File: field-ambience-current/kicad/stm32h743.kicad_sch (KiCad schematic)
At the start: 33 parts, among them J10 3.5mm TRS MIDI-Out (Type A, P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, J4 SWD 1.27mm (SWCLK/GND/SWDIO), U1 STM32H743VIT6 (480MHz M7, LQF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, Y1 8MHz ABLS-8.000MHZ-B4-T (CL=1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

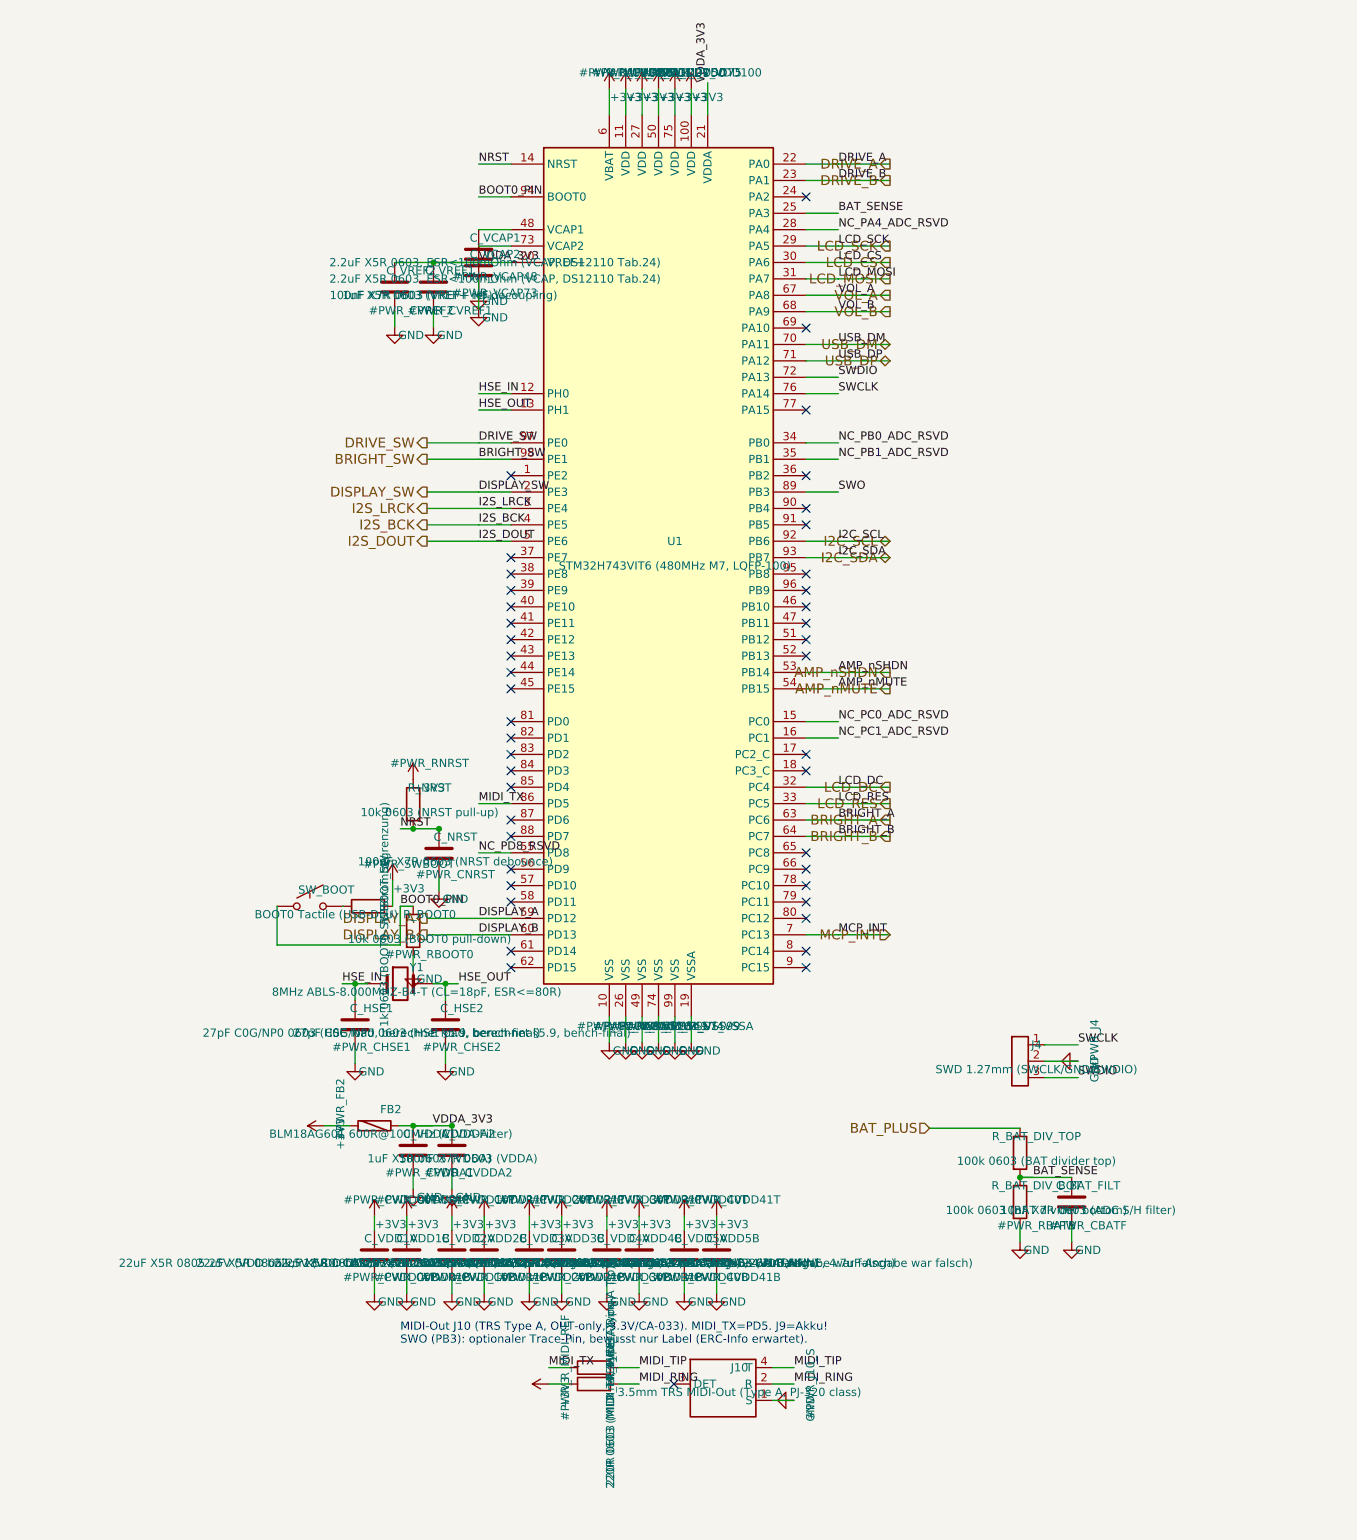
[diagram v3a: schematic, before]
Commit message: feat(hw): QSPI-PSRAM 8MB (APS6404L) into the schematic on QUADSPI BK2 (r19.10)
* feat(hw): QSPI-PSRAM (8MB) into the schematic — U9 APS6404L on QUADSPI BK2 (r19.10)

Implements ADR-0022. The internal RAM is the wall for "maximum sound"
(D1/D2 at 96%); this adds an external 8 MB QSPI PSRAM, memory-mapped over
QUADSPI Bank 2, so the CPU reads it like internal RAM (behind the D-cache).
Enables sample playback, convolution reverb with real IRs, big granular,
and a true multi-table Blendwave — megabytes instead of kilobytes.

Generator (generate_kicad_project.py, stm32h743 sheet):
- New lib_symbol Memory_RAM:APS6404L (SOP-8). Pinout VERIFIED against the AP
  Memory datasheet Rev 2.1 (2019), top view: 1=/CE 2=SO/SIO1 3=SIO2 4=VSS
  5=SI/SIO0 6=SCLK 7=SIO3 8=VDD.
- U9 APS6404L-3SQR-SN, FP Package_SO:SOIC-8_3.9x4.9mm_P1.27mm (dimensionally
  matches SOP-8L(150) = 3.9mm body / 1.27mm pitch; standard SOIC pad
  numbering), LCSC C5333729. FP_NOTE recommends pulling the exact LCSC land
  pattern via easyeda2kicad as a belt-and-suspenders final check.
- 6 QSPI nets on the MCU pins PB2(36)/PC11(79)/PE7-10(37-40):
  QSPI_CLK/QSPI_NCS/QSPI_IO0-3, wired both sides by local label.
- Decoupling C_QSPI 100nF (C14663) + C_QSPI2 10uF (C15850) to +3V3/GND;
  U9 VDD->+3V3, VSS->GND.

Docs/BOM:
- PINMAP: PB2/PC11/PE7-10 marked as QSPI (no longer free) + connectivity
  table; fixed ADR "Pin 80" -> PC11 is LQFP100 pin 79 (pin 80 = PC12).
- jlc_bom.csv regenerated (U9 + 2 caps flow from the schematic).
- bom_overview.html: new "Memory" group; U9 badge honestly "JLC ? verify"
  (JLC-Economic assemblable per ADR — verify live before order).
- ADR-0022 -> IMPLEMENTED with datasheet-verified pinout + Verifikation.

Verification: kicad-cli 7.0.11 in this environment cannot load the
generated schematic (Failed to load schematic file — reproduced on the
UNCHANGED baseline via git stash, so it is a pre-existing parser
incompatibility, not this change) and has no `sch erc` subcommand. Verified
at text 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
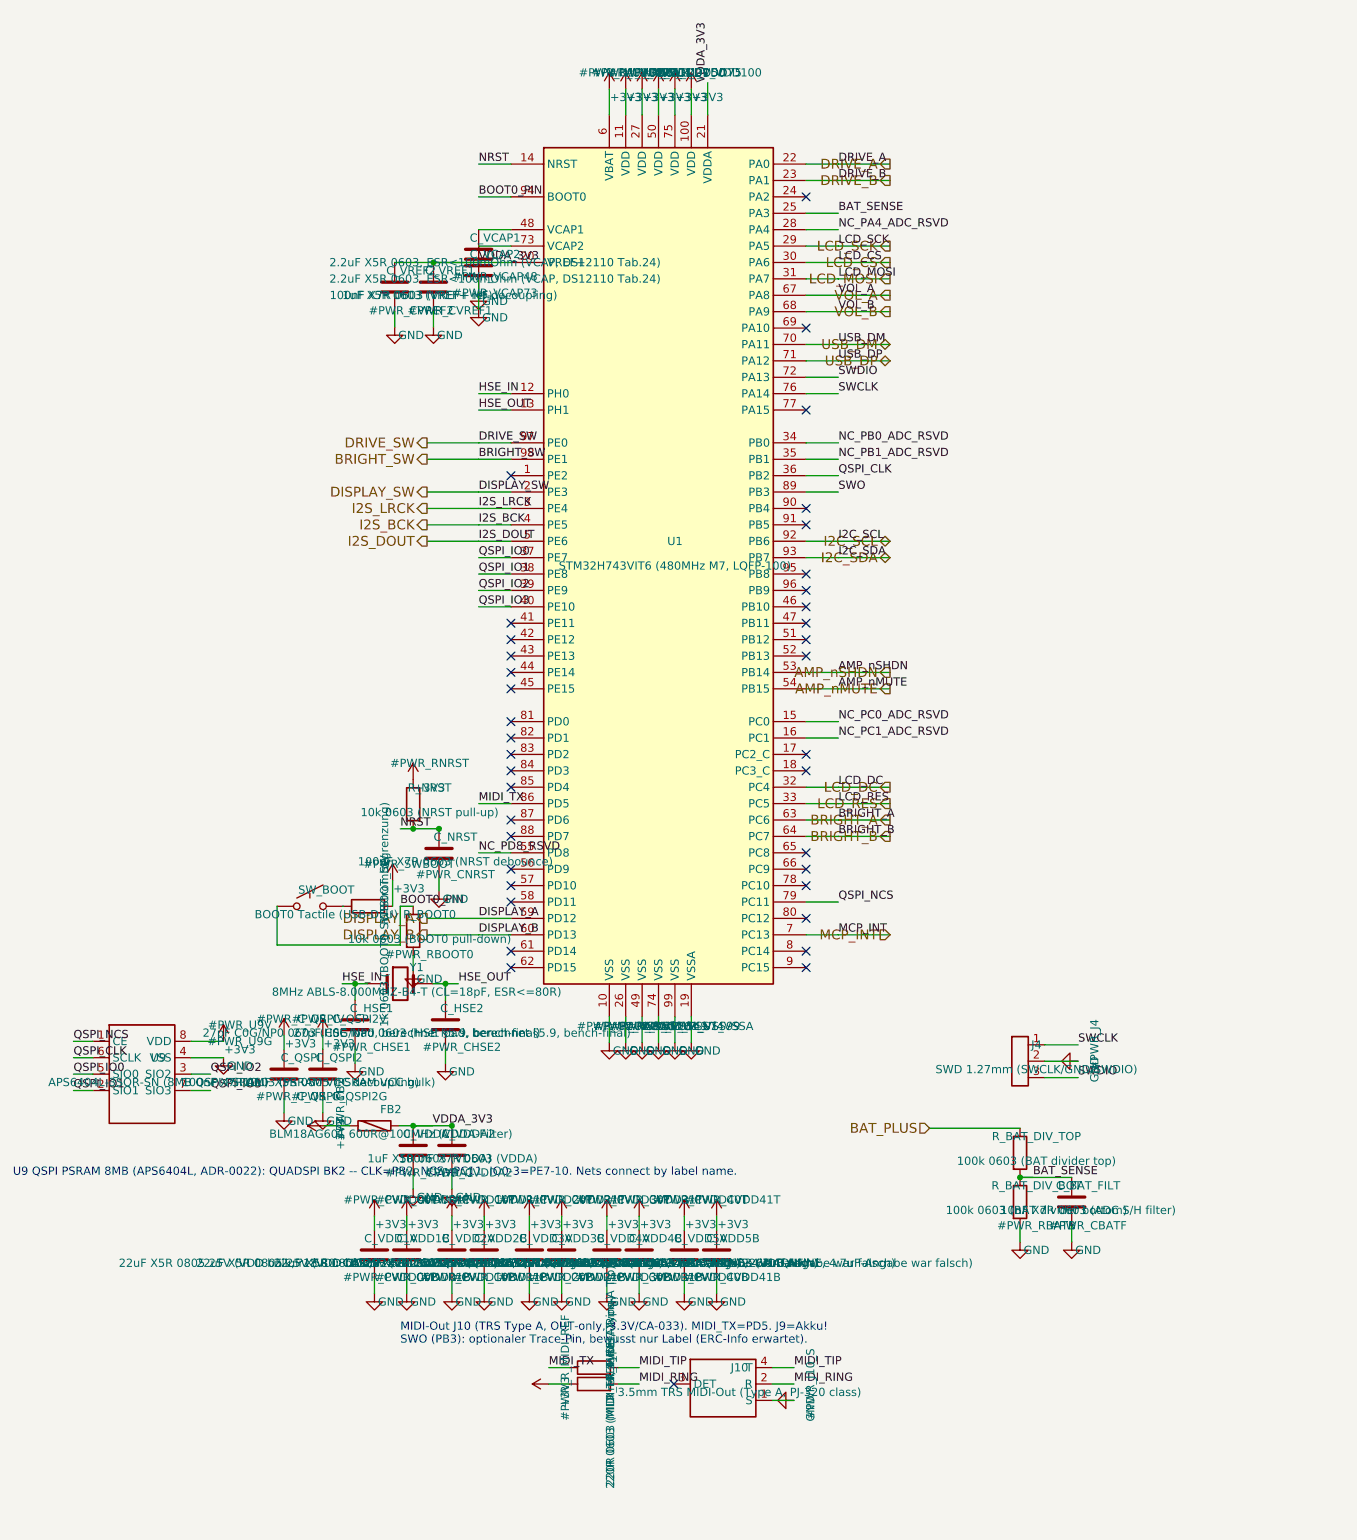
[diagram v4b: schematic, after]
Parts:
- added C_QSPI: 100nF X7R 0603 (PSRAM VCC decoupling), Capacitor_SMD:C_0603_1608Metric, symbol Device:C
- added C_QSPI2: 10uF X5R 0805 (PSRAM VCC bulk), Capacitor_SMD:C_0805_2012Metric, symbol Device:C
- added U9: APS6404L-3SQR-SN (8MB QSPI PSRAM), Package_SO:SOIC-8_3.9x4.9mm_P1.27mm, symbol Memory_RAM:APS6404L
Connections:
- net +3V3: now also C_QSPI.1, C_QSPI2.1, U9.8 (VDD)
- net GND: now also C_QSPI.2, C_QSPI2.2, U9.4 (VSS)
- net QSPI_CLK: now reaches U1.36 (PB2)
- net QSPI_CLK: now also U9.6 (SCLK)
- net QSPI_IO0: now reaches U1.37 (PE7)
- net QSPI_IO0: now also U9.5 (SIO0)
- net QSPI_IO1: now reaches U1.38 (PE8)
- net QSPI_IO1: now also U9.2 (SIO1)
- net QSPI_IO2: now reaches U1.39 (PE9)
- net QSPI_IO2: now also U9.3 (SIO2)
- net QSPI_IO3: now reaches U1.40 (PE10)
- net QSPI_IO3: now also U9.7 (SIO3)
- net QSPI_NCS: now reaches U1.79 (PC11)
- net QSPI_NCS: now also U9.1 (CE)
- no-connect marks 44 -> 38
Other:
- note added: "U9 QSPI PSRAM 8MB (APS6404L, ADR-0022): QUADSPI BK2 -- CLK=PB2, NCS=PC11, IO0-3=PE7-10. Nets connect by label name."

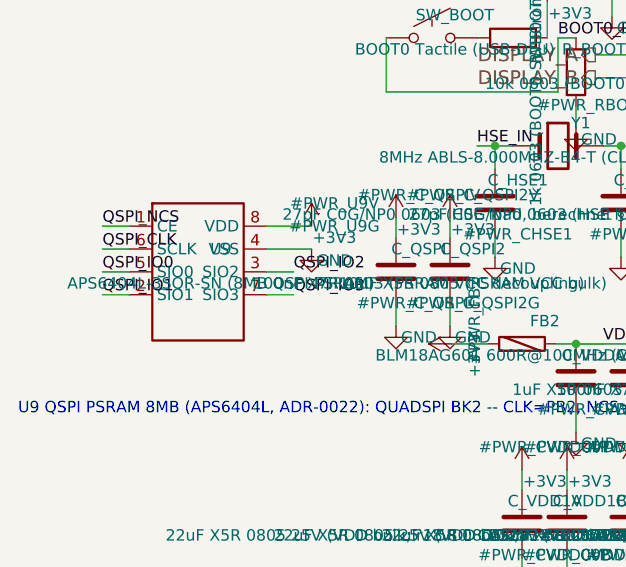
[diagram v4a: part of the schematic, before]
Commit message: fix(bom): PSRAM out of stock — swap C5333729 (3SQR-SN) → C3028887 (3SQN-SN), live-verified
APS6404L-3SQR-SN (C5333729) is "Not available now" at LCSC/JLC (confirmed on
the live product page 2026-07-07). Replacement verified live today:
APS6404L-3SQN-SN, LCSC C3028887 — same AP Memory 3V family (2.7-3.6V, the
critical check: the in-stock SQN-SN C5360304 is the 1.8V variant and would NOT
work on our +3V3 rail), same SOP-8 pinout/footprint, 133 MHz, LCSC 432 in
stock "ships now" ($4.52@1 / $3.09@100), JLC Economic+Standard assemblable.

Generator + schematic + jlc_bom.csv + bom_overview + ADR-0022 + COMPONENT_LINKS
+ OBJECTIVES doc all updated; check_pinmap OK; old C-number fully gone from the
BOM.

Co-Authored-By: Claude Fable 5 <noreply@anthropic.com>
Claude-Session: https://claude.ai/code/session_019pKguH6aG4iazMCWJnpmMn
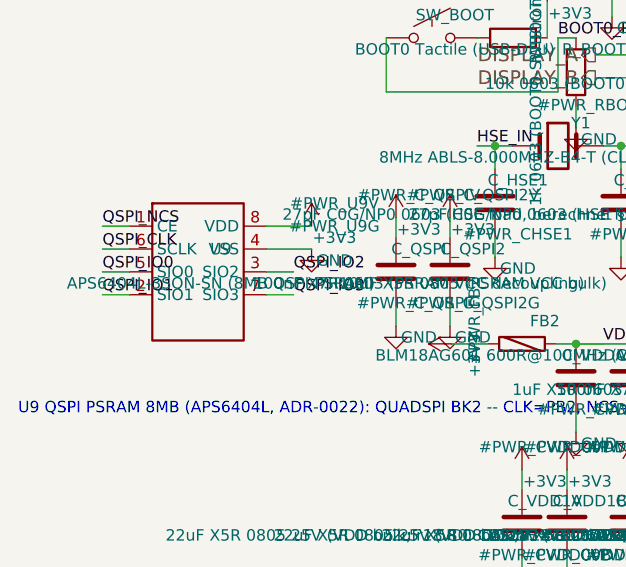
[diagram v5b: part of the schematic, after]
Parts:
- U9: value APS6404L-3SQR-SN (8MB QSPI PSRAM) -> APS6404L-3SQN-SN (8MB QSPI PSRAM); FP_NOTE SOP-8L(150) = 3.9mm body / 1.27mm pitch. ADR-0022. Pinout VERIFIED vs AP Memory datasheet Rev 2.1 (2019): 1=/CE 2=SO/SIO1 3=SIO2 4=VSS 5=SI/SIO0 6=SCLK 7=SIO3 8=VDD. FP dims match generic SOIC-8_3.9x4.9_P1.27 (std pad numbering). Belt+suspenders: pull exact LCSC land pattern via easyeda2kicad --full --lcsc_id=C5333729 before fab. -> SOP-8L(150) = 3.9mm body / 1.27mm pitch. ADR-0022. Pinout VERIFIED vs AP Memory datasheet Rev 2.1 (2019): 1=/CE 2=SO/SIO1 3=SIO2 4=VSS 5=SI/SIO0 6=SCLK 7=SIO3 8=VDD. FP dims match generic SOIC-8_3.9x4.9_P1.27 (std pad numbering). Belt+suspenders: pull exact LCSC land pattern via easyeda2kicad --full --lcsc_id=C3028887 before fab.; LCSC C5333729 -> C3028887; MPN APS6404L-3SQR-SN -> APS6404L-3SQN-SN
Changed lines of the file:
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@@
       (property "Reference" "U9" (at 62.54 207.46 0)
         (effects (font (size 1.27 1.27))))
-      (property "Value" "APS6404L-3SQR-SN (8MB QSPI PSRAM)" (at 62.54 211.27 0)
+      (property "Value" "APS6404L-3SQN-SN (8MB QSPI PSRAM)" (at 62.54 211.27 0)
         (effects (font (size 1.27 1.27))))
       (property "Footprint" "Package_SO:SOIC-8_3.9x4.9mm_P1.27mm" (at 60.0 210.0 0)
         (effects (font (size 1.27 1.27)) hide))
-      (property "Datasheet" "https://www.lcsc.com/product-detail/C5333729.html" (at 60.0 210.0 0)
+      (property "Datasheet" "https://www.lcsc.com/product-detail/C3028887.html" (at 60.0 210.0 0)
         (effects (font (size 1.27 1.27)) hide))
-      (property "MPN" "APS6404L-3SQR-SN" (at 62.54 213.81 0)
+      (property "MPN" "APS6404L-3SQN-SN" (at 62.54 213.81 0)
         (effects (font (size 1.27 1.27)) hide))
-      (property "LCSC" "C5333729" (at 62.54 215.08 0)
+      (property "LCSC" "C3028887" (at 62.54 215.08 0)
         (effects (font (size 1.27 1.27)) hide))
-      (property "FP_NOTE" "SOP-8L(150) = 3.9mm body / 1.27mm pitch. ADR-0022. Pinout VERIFIED vs AP Memory datasheet Rev 2.1 (2019): 1=/CE 2=SO/SIO1 3=SIO2 4=VSS 5=SI/SIO0 6=SCLK 7=SIO3 8=VDD. FP dims match generic SOIC-8_3.9x4.9_P1.27 (std pad numbering). Belt+suspenders: pull exact LCSC land pattern via easyeda2kicad --full --lcsc_id=C5333729 before fab." (at 62.54 216.35 0)
+      (property "FP_NOTE" "SOP-8L(150) = 3.9mm body / 1.27mm pitch. ADR-0022. Pinout VERIFIED vs AP Memory datasheet Rev 2.1 (2019): 1=/CE 2=SO/SIO1 3=SIO2 4=VSS 5=SI/SIO0 6=SCLK 7=SIO3 8=VDD. FP dims match generic SOIC-8_3.9x4.9_P1.27 (std pad numbering). Belt+suspenders: pull exact LCSC land pattern via easyeda2kicad --full --lcsc_id=C3028887 before fab." (at 62.54 216.35 0)
         (effects (font (size 1.27 1.27)) hide))
     (instances

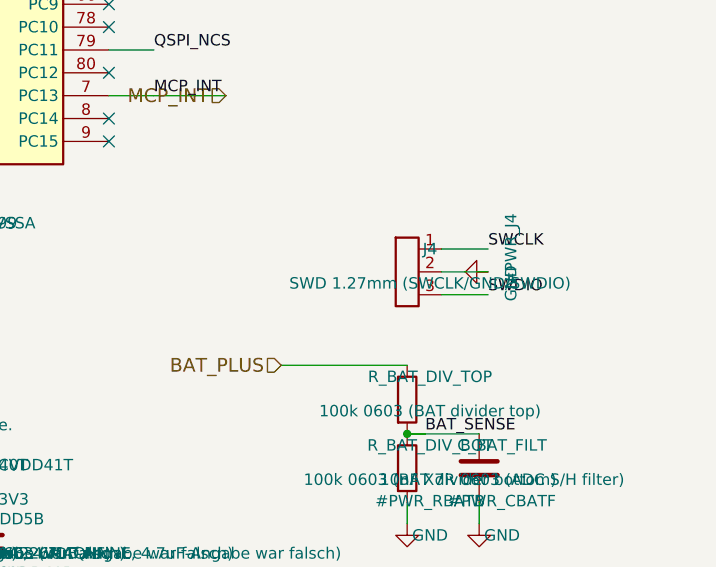
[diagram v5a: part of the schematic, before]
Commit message: feat(hw): BQ24074 power-path replaces MCP73831 + diode-OR — all audit P0 fixed (r19.18, ADR-0023)
External hardware audit verdict was DO NOT FABRICATE; every checkable P0
was confirmed against the extracted netlist, then fixed at the generator:

- U7 = BQ24074RGTR (C54313, live-verified stock + JLC assembly):
  USB->F1->VBUS_FUSED->IN; OUT=VSYS->TPS61089->D3->+5V rail (single
  source, D3B diode-OR deleted); BAT<-F2 PTC (SMD1812P260TF/16,
  C438899)<-J9. Values per TI SLUS810N: ICHG 0.89A (R_ISET 1k),
  IIN 1.34A (R_ILIM_IN 1.2k YAGEO C114605), ITERM/TMR=NC defaults,
  TS=10k fixed, EN2=VSYS/EN1=GND, CE_N=GND, EP->VSS.
- Boost EN = PWR_ON (was always-on battery drain); SW_PWR pull source
  moved to VSYS (rail-sourced pull would deadlock); LED_CHRG now fed
  from VBUS_FUSED via CHG open-drain; rail bulk sits behind the boost
  (USB hot-plug sees only 4.7uF).
- New inter-sheet nets VBUS_FUSED/VSYS/PWR_ON via root; +5V_OUT is now
  an input on the power tree. TP_VSYS test point added.
- Footprint QFN-16-1EP_3x3mm_P0.5mm_EP1.7x1.7mm matched against the
  JLC/EasyEDA land pattern for C54313 (pitch/pads/EP identical).
- J4 SWD = DNP debug pads (bogus TC2030-IDC MPN + LCSC "TBD" removed
  from the order BOM); J8 explicitly LINE OUT; mechanical doc battery
  corrected 5000->2000 mAh.
- Validation: geometric netlist extractor over all 7 sheets — 157 nets,
  620 pins, 0 floating; check_pinmap green; host suite green (32 suites).
- Docs: ADR-0023, CHANGELOG r19.18, PROJECT_STATUS banner, SCHEMATIC_
  WALKTHROUGH §1/§7 rewritten, PINMAP/BRING_UP/BOM_MASTER/PCB_BOM/
  COST/SOURCING/OBJECTIVES/COMPONENT_LINKS/FOOTPRINT_RISK updated.

Co-Authored-By: Claude Fable 5 <noreply@anthropic.com>
Claude-Session: https://claude.ai/code/session_019pKguH6aG4iazMCWJnpmMn
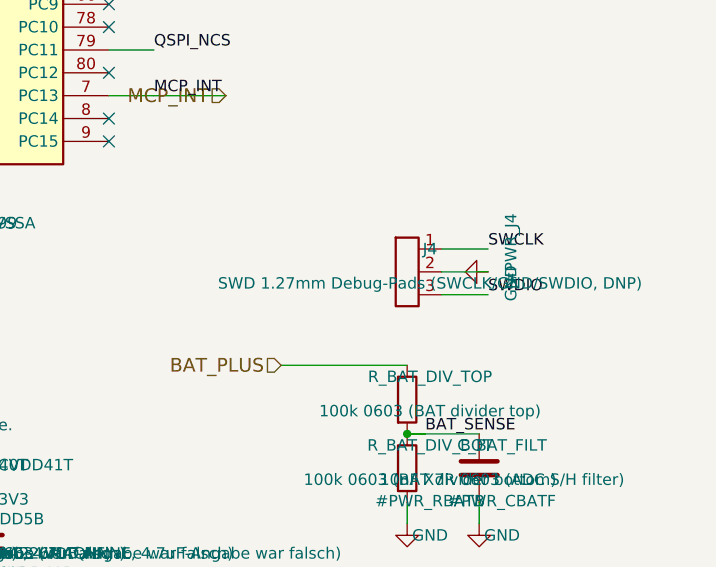
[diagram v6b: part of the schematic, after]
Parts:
- J4: value SWD 1.27mm (SWCLK/GND/SWDIO) -> SWD 1.27mm Debug-Pads (SWCLK/GND/SWDIO, DNP); DNP (none) -> true (Debug-Pads; Header bei Bedarf von Hand: beliebiger 1x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; LCSC TBD -> (none); MPN TC2030-IDC -> (none); NOTE (none) -> r19.18: Ex-MPN TC2030-IDC entfernt (war das Tag-Connect-Kab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
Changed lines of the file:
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@@
       (property "Reference" "J4" (at 198.54 205.46 0)
         (effects (font (size 1.27 1.27))))
-      (property "Value" "SWD 1.27mm (SWCLK/GND/SWDIO)" (at 198.54 209.27 0)
+      (property "Value" "SWD 1.27mm Debug-Pads (SWCLK/GND/SWDIO, DNP)" (at 198.54 209.27 0)
         (effects (font (size 1.27 1.27))))
       (property "Footprint" "Connector_PinHeader_1.27mm:PinHeader_1x03_P1.27mm_Vertical" (at 196.0 208.0 0)
@@
       (property "Datasheet" "~" (at 196.0 208.0 0)
         (effects (font (size 1.27 1.27)) hide))
-      (property "MPN" "TC2030-IDC" (at 198.54 211.81 0)
+      (property "DNP" "true (Debug-Pads; Header bei Bedarf von Hand: beliebiger 1x3 P1.27mm vertikal)" (at 198.54 211.81 0)
         (effects (font (size 1.27 1.27)) hide))
-      (property "LCSC" "TBD" (at 198.54 213.08 0)
+      (property "NOTE" "r19.18: Ex-MPN TC2030-IDC entfernt (war das Tag-Connect-Kabel, nicht dieser Header)." (at 198.54 213.08 0)
         (effects (font (size 1.27 1.27)) hide))
     (instances
